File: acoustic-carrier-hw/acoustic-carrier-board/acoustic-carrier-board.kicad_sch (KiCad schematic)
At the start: 0 parts

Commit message: [carrier] Routed 6x2 IO connector
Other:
- sheet CONNECTORS ports: added PMOD_IO{PMOD_IO}; removed none
- sheet FPGA-DQBANK-67 ports: added PMOD_IO{PMOD_IO}; removed none
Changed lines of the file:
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@@
+	(bus
+		(pts
+			(xy 223.52 97.79) (xy 226.06 97.79)
+		)
+		(stroke
+			(width 0)
+			(type default)
+		)
+	)
 	(bus
 		(pts
@@
 		(pts
 			(xy 59.69 100.33) (xy 60.96 100.33)
+		)
+		(stroke
+			(width 0)
+			(type default)
+		)
+	)
+	(bus
+		(pts
+			(xy 173.99 48.26) (xy 176.53 48.26)
 		)
 		(stroke
@@
 		)
 	)
+	(label "PMOD_IO{PMOD_IO}"
+		(at 223.52 97.79 180)
+		(effects
+			(font
+				(size 1.27 1.27)
+			)
+			(justify right bottom)
+		)
+	)
 	(label "RGMII_TX{RGMII_TX}"
 		(at 60.96 96.52 0)
@@
 			)
 			(justify right bottom)
+		)
+	)
+	(label "PMOD_IO{PMOD_IO}"
+		(at 176.53 48.26 0)
+		(effects
+			(font
+				(size 1.27 1.27)
+			)
+			(justify left bottom)
 		)
 	)
@@
 			)
 		)
+		(pin "PMOD_IO{PMOD_IO}" bidirectional
+			(at 173.99 48.26 0)
+			(effects
+				(font
+					(size 1.27 1.27)
+				)
+				(justify right)
+			)
+		)
 		(instances
 			(project "acoustic-carrier-board"
@@
 			(effects
 				(font
+					(size 1.27 1.27)
+				)
+				(justify left)
+			)
+		)
+		(pin "PMOD_IO{PMOD_IO}" bidirectional
+			(at 226.06 97.79 180)
+			(effects
+				(font

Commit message: [carrier] Routed out signals for board-to-board PTH
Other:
- sheet CONNECTORS ports: added SIGCON{SIGCON}; removed CON1{SIGCON1}
- sheet FPGA-BANK-01 ports: added SIGCON{SIGCON}; removed none
- sheet FPGA-DQBANK-67 ports: added none; removed CON1{SIGCON1}
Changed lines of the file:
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@@
+	(bus
+		(pts
+			(xy 175.26 92.71) (xy 179.07 92.71)
+		)
+		(stroke
+			(width 0)
+			(type default)
+		)
+	)
 	(bus
 		(pts
@@
 		(pts
 			(xy 175.26 67.31) (xy 199.39 67.31)
-		)
-		(stroke
-			(width 0)
-			(type default)
-		)
-	)
-	(bus
-		(pts
-			(xy 173.99 52.07) (xy 176.53 52.07)
 		)
 		(stroke
@@
 		)
 	)
-	(label "CON1{SIGCON1}"
+	(label "SIGCON{SIGCON}"
 		(at 223.52 92.71 180)
 		(effects
@@
 		)
 	)
-	(label "CON1{SIGCON1}"
-		(at 176.53 52.07 0)
+	(label "SIGCON{SIGCON}"
+		(at 179.07 92.71 0)
 		(effects
 			(font
@@
 			)
 		)
+		(pin "SIGCON{SIGCON}" bidirectional
+			(at 175.26 92.71 0)
+			(effects
+				(font
+					(size 1.27 1.27)
+				)
+				(justify right)
+			)
+		)
 		(instances
 			(project "acoustic-carrier-board"
@@
 			)
 		)
-		(pin "CON1{SIGCON1}" bidirectional
-			(at 173.99 52.07 0)
-			(effects
-				(font
-					(size 1.27 1.27)
-				)
-				(justify right)
-			)
-		)
 		(pin "RGMII_RX{RGMII_RX}" input
 			(at 123.19 50.8 180)
@@
 			)
 		)
-		(pin "CON1{SIGCON1}" bidirectional
+		(pin "SIGCON{SIGCON}" bidirectional
 			(at 226.06 92.71 180)
 			(effects

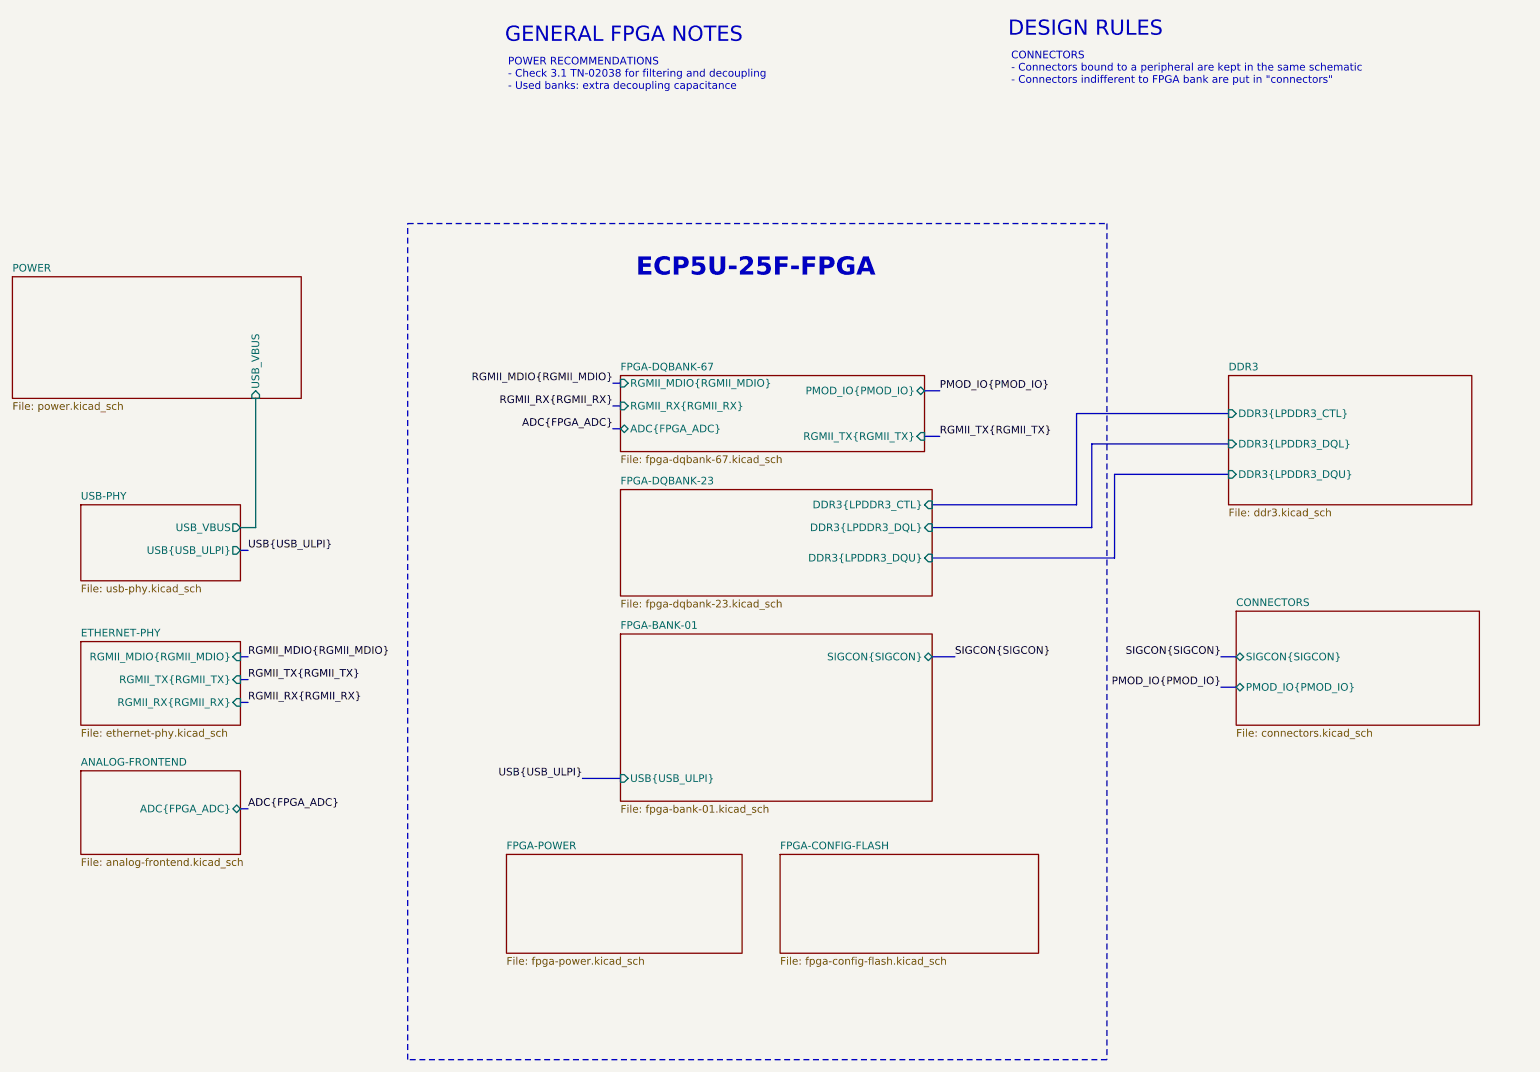
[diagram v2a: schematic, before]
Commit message: [carrier] Fixed last errors, redid length matching for LPDDR3
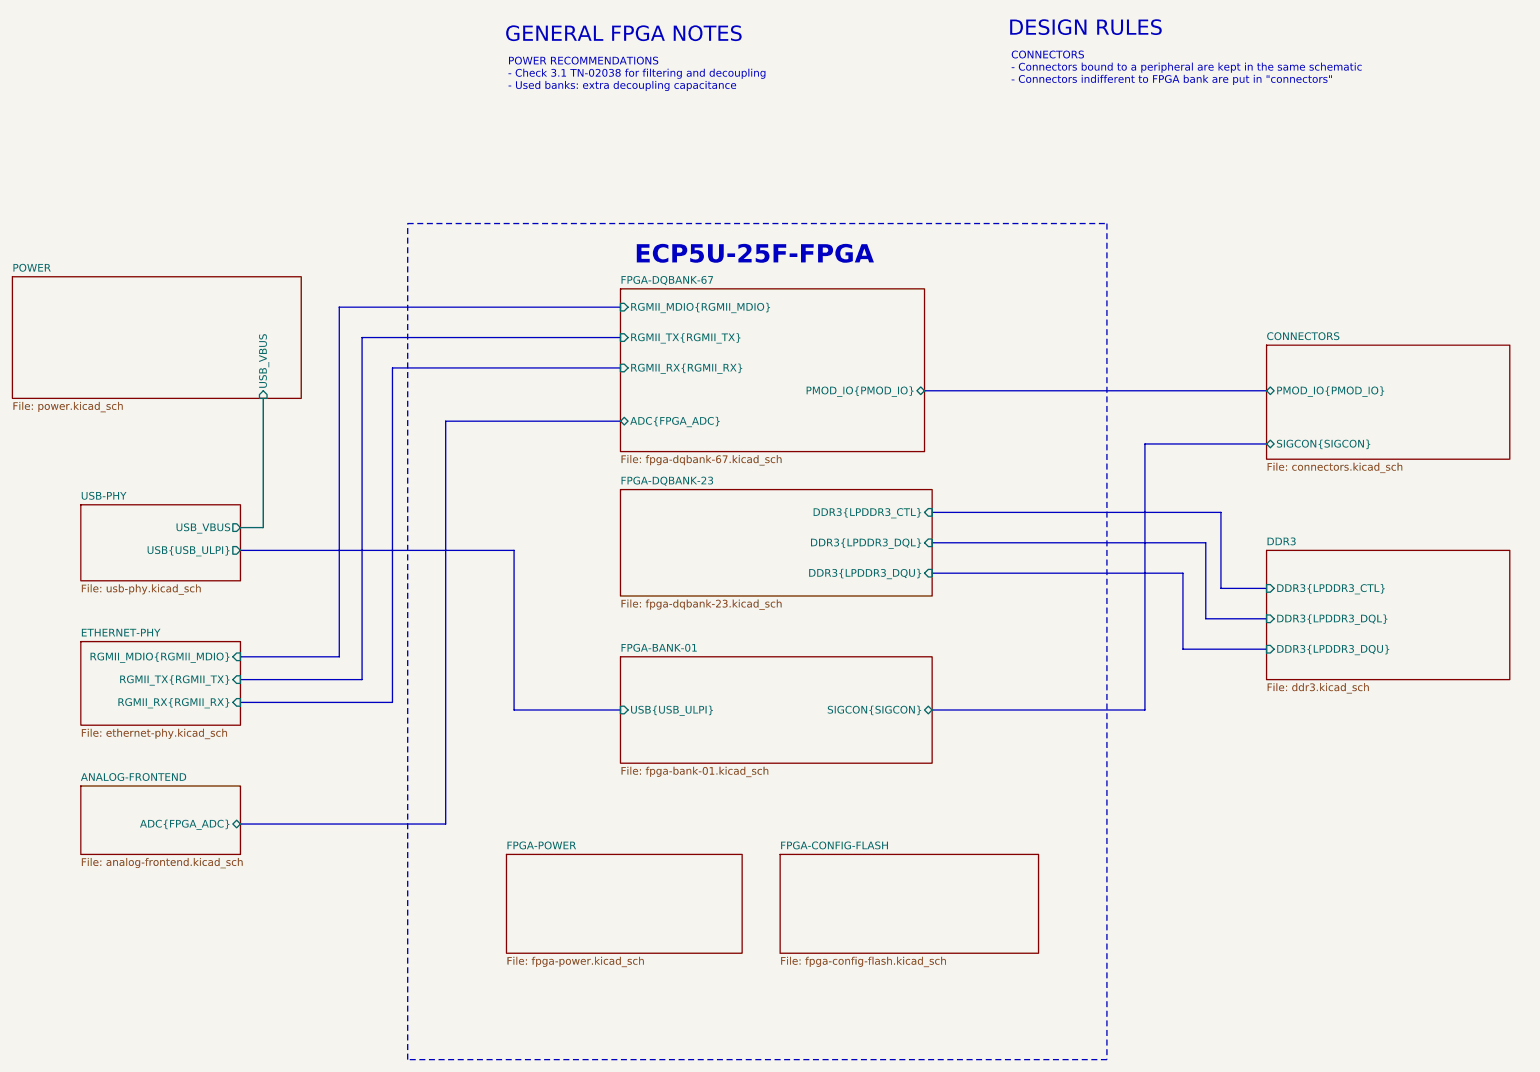
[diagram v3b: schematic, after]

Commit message: [carrier] finished final review, (next) posting to linkedin, start working on analog front-end board
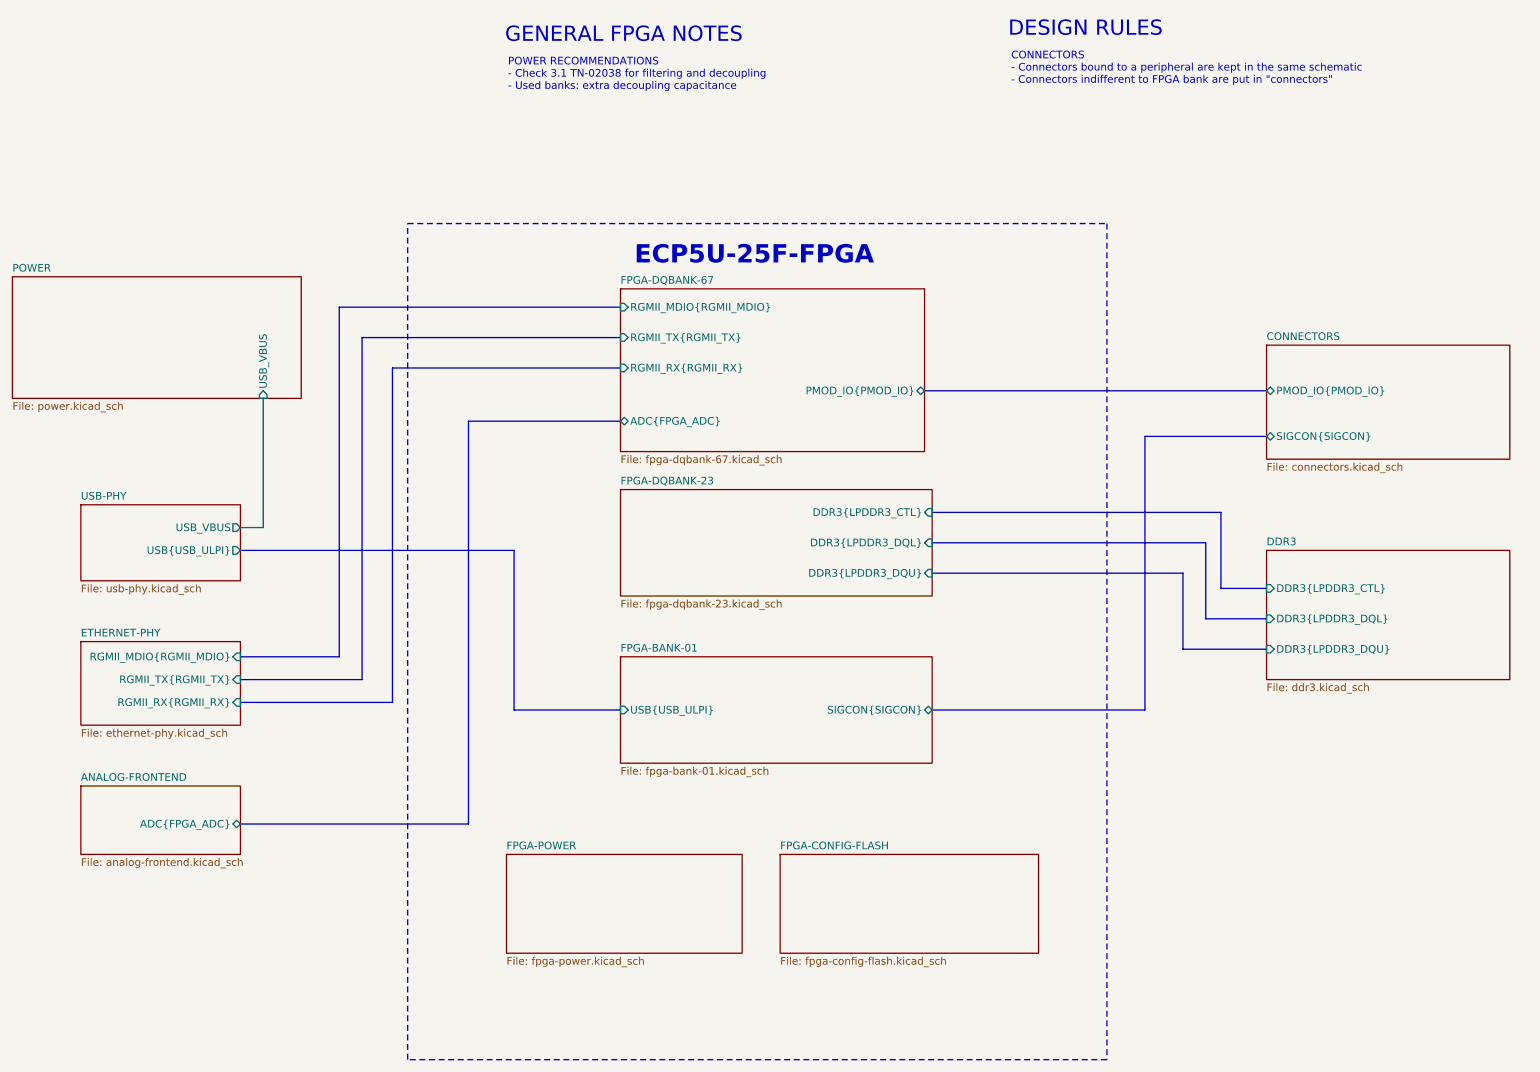
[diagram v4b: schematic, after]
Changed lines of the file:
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@@
 	(bus
 		(pts
-			(xy 123.19 53.34) (xy 93.98 53.34)
+			(xy 123.19 53.34) (xy 97.79 53.34)
 		)
 		(stroke
@@
 	(bus
 		(pts
-			(xy 210.82 101.6) (xy 210.82 57.15)
-		)
-		(stroke
-			(width 0)
-			(type default)
-		)
-	)
-	(bus
-		(pts
-			(xy 59.69 120.65) (xy 93.98 120.65)
+			(xy 210.82 101.6) (xy 210.82 55.88)
+		)
+		(stroke
+			(width 0)
+			(type default)
+		)
+	)
+	(bus
+		(pts
+			(xy 59.69 120.65) (xy 97.79 120.65)
 		)
 		(stroke
@@
 	(bus
 		(pts
-			(xy 210.82 57.15) (xy 231.14 57.15)
+			(xy 210.82 55.88) (xy 231.14 55.88)
 		)
 		(stroke
@@
 	(bus
 		(pts
-			(xy 93.98 53.34) (xy 93.98 120.65)
+			(xy 97.79 53.34) (xy 97.79 120.65)
 		)
 		(stroke
@@
 		)
 		(pin "SIGCON{SIGCON}" bidirectional
-			(at 231.14 57.15 180)
-			(effects
-				(font
+			(at 231.14 55.88 180)
+			(effects
+				(font

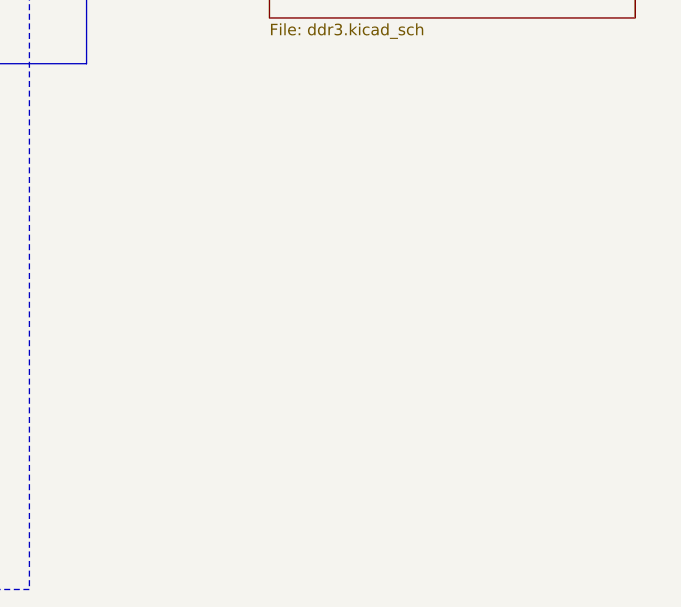
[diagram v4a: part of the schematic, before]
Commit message: [carrier] finished for production (next) reroute the LPDDR3, with appropriate CMD-CTRL bus delays, and change banks for command-control
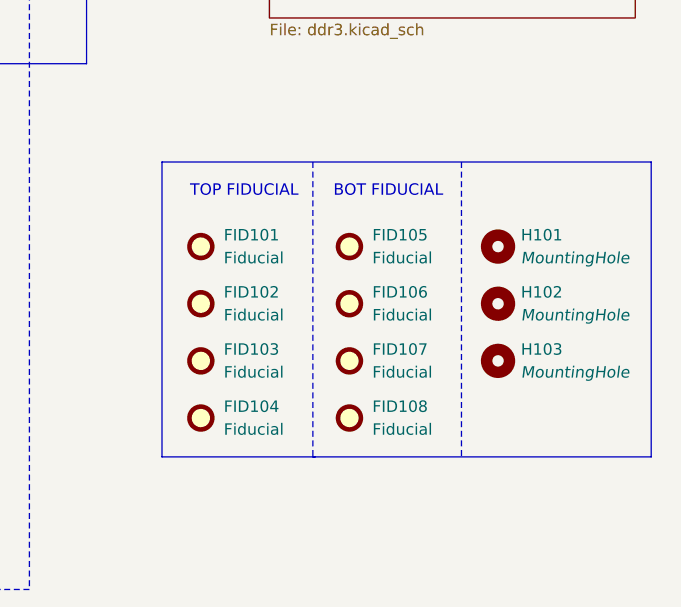
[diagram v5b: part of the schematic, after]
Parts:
- added FID101, FID102, FID103, FID104, FID105, FID106, FID107, FID108: Fiducial, Fiducial:Fiducial_1mm_Mask2mm, symbol Mechanical:Fiducial
- added H101, H102, H103: MountingHole, MountingHole:ToolingHole_1.152mm, symbol Mechanical:MountingHole
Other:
- note added: "BOT FIDUCIAL"
- note added: "TOP FIDUCIAL"
